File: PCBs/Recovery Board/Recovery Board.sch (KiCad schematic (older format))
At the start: 23 parts, among them J1 Conn_01x02, J2 Conn_01x02, J3 Conn_01x02, J4 Conn_01x02, J5 Conn_01x02, J6 Conn_01x02, U1 R-78E3.3-0.5, X1 XBee-S2C

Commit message: swapped all mounting holes with plated ones, fixed disconnected components on recovery, added the 4 decoupling caps to recovery, fixed silk screen on pads in instr, fixed traces connecting through pads on recovery and instr, moved q1 on instr, brought trace in near u2 on instr, switched u2 & u3 to hand solder on instr, fixed xbee screen on recovery, fixed connector labels on recovery, removed recovery dims past edge cuts, fixed pad mask clearance on recovery
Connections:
- net Stratologger_Switch+: now also J3.1 (Pin_1), S2.4 (DC_+); no longer J3.2 (Pin_2), S2.3 (DC_-)
- net Stratologger_Switch-: now also J3.2 (Pin_2), S2.3 (DC_-); no longer J3.1 (Pin_1), S2.4 (DC_+)
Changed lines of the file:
@@
 LIBS:fgpmmopa6h
 LIBS:sot-223
+LIBS:Placeholders
 LIBS:Recovery Board Parts
 LIBS:ap2204k-5
 LIBS:Recovery Board-cache
 LIBS:instrumentation_board_parts
+LIBS:instrumentation_board-cache
 EELAYER 25 0
 EELAYER END
@@
 	1    0    0    -1
 $EndComp
+Text GLabel 7550 1300 2    60   Input Italic 0
+Stratologger_Switch-
 Text GLabel 7550 900  2    60   Input Italic 0
-Stratologger_Switch-
-Text GLabel 7550 1300 2    60   Input Italic 0
 Stratologger_Switch+
 Text GLabel 2600 3300 2    60   Input ~ 0
@@
 Text GLabel 2600 2700 2    60   Input Italic 0
 Intrument_Arduino_Power
+Text GLabel 2600 2000 2    60   Input Italic 0
+Stratologger_Switch+
 Text GLabel 2600 2100 2    60   Input Italic 0
-Stratologger_Switch+
-Text GLabel 2600 2000 2    60   Input Italic 0
 Stratologger_Switch-
 $Comp

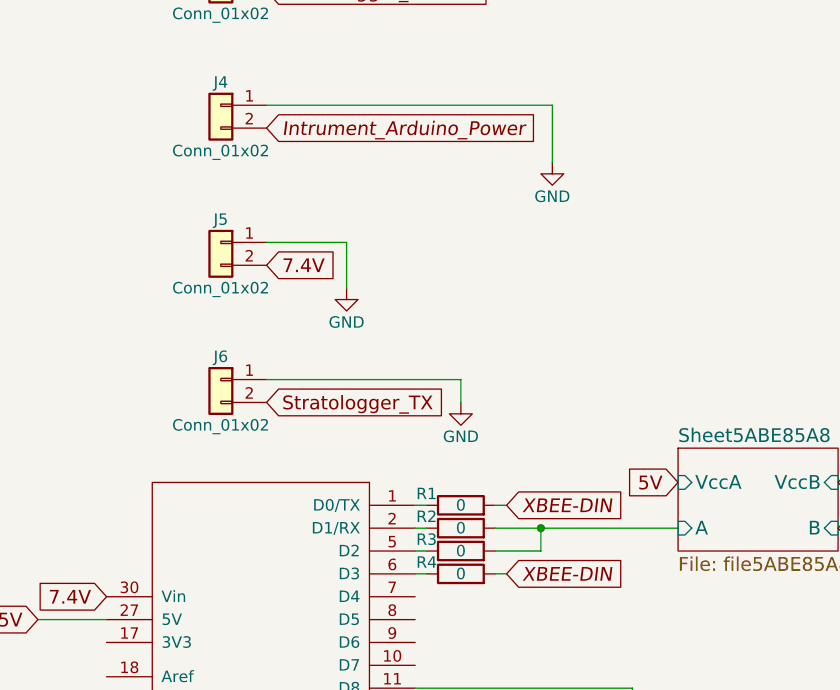
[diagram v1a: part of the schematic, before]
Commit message: Changed connectors for recovery board batteries
Added a second connector for the other battery
Moved connectors to top of board
Replaced footprint with JST-PH
Extended board width
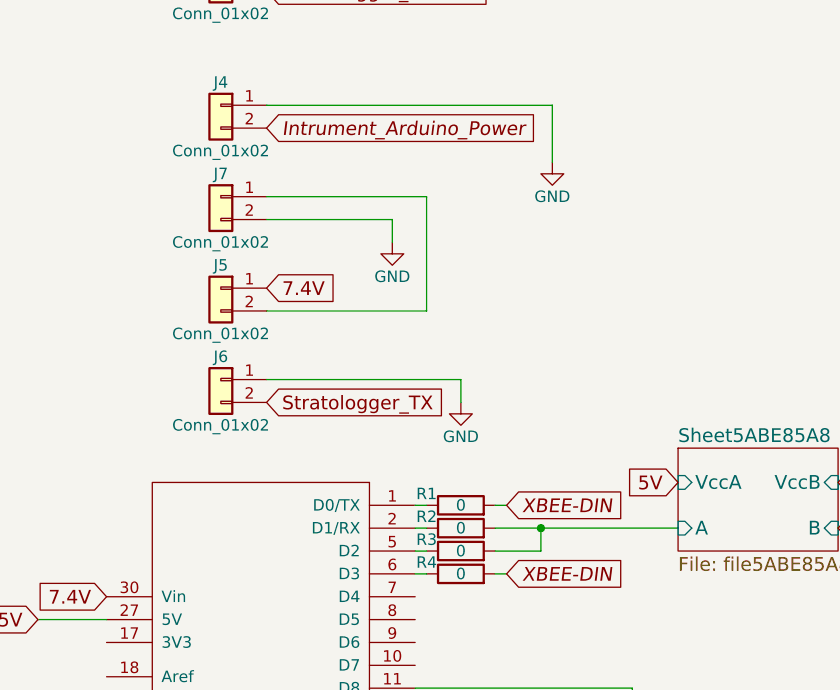
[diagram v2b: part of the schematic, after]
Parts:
- added J7: Conn_01x02, Connectors_JST:JST_PH_B2B-PH-K_02x2.00mm_Straight, symbol Conn_01x02
- J5: footprint Connectors_Molex:Molex_KK-6410-02_02x2.54mm_Straight -> Connectors_JST:JST_PH_B2B-PH-K_02x2.00mm_Straight
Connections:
- net 7.4V: now also J5.1 (Pin_1); no longer J5.2 (Pin_2)
- net GND: now also J7.2 (Pin_2); no longer J5.1 (Pin_1)
- new net: J5.2 (Pin_2), J7.1 (Pin_1)
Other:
- moved on the sheet: J5
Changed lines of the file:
@@
 Text GLabel 7550 900  2    60   Input Italic 0
 Stratologger_Switch+
-Text GLabel 2600 3300 2    60   Input ~ 0
+Text GLabel 2600 3400 2    60   Input ~ 0
 7.4V
 Text GLabel 7450 2000 2    60   Input ~ 0
@@
 L Conn_01x02 J5
 U 1 1 5A9A1806
-P 2400 3200
-F 0 "J5" H 2400 3300 50  0000 C CNN
-F 1 "Conn_01x02" H 2400 3000 50  0000 C CNN
-F 2 "Connectors_Molex:Molex_KK-6410-02_02x2.54mm_Straight" H 2400 3200 50  0001 C CNN
-F 3 "" H 2400 3200 50  0001 C CNN
-	1    2400 3200
+P 2400 3400
+F 0 "J5" H 2400 3500 50  0000 C CNN
+F 1 "Conn_01x02" H 2400 3200 50  0000 C CNN
+F 2 "Connectors_JST:JST_PH_B2B-PH-K_02x2.00mm_Straight" H 2400 3400 50  0001 C CNN
+F 3 "" H 2400 3400 50  0001 C CNN
+	1    2400 3400
 	-1   0    0    -1
 $EndComp
@@
 $EndComp
 $Comp
-L GND #PWR010
-U 1 1 5A9AE056
-P 2950 3400
-F 0 "#PWR010" H 2950 3150 50  0001 C CNN
-F 1 "GND" H 2950 3250 50  0000 C CNN
-F 2 "" H 2950 3400 50  0001 C CNN
-F 3 "" H 2950 3400 50  0001 C CNN
-	1    2950 3400
-	1    0    0    -1
-$EndComp
-$Comp
 L C C1
 U 1 1 5A9AEA7D
@@
 GoPro_Power
 $Comp
-L GND #PWR011
+L GND #PWR010
 U 1 1 5A9AF05A
 P 3850 2850
-F 0 "#PWR011" H 3850 2600 50  0001 C CNN
+F 0 "#PWR010" H 3850 2600 50  0001 C CNN
 F 1 "GND" H 3850 2700 50  0000 C CNN
 F 2 "" H 3850 2850 50  0001 C CNN
@@
 $EndComp
 $Comp
-L GND #PWR012
+L GND #PWR011
 U 1 1 5A9AF30B
 P 3350 1500
-F 0 "#PWR012" H 3350 1250 50  0001 C CNN
+F 0 "#PWR011" H 3350 1250 50  0001 C CNN
 F 1 "GND" H 3350 1350 50  0000 C CNN
 F 2 "" H 3350 1500 50  0001 C CNN
@@
 $EndComp
 $Comp
-L GND #PWR013
+L GND #PWR012
 U 1 1 5ABA400A
 P 8250 4650
-F 0 "#PWR013" H 8250 4400 50  0001 C CNN
+F 0 "#PWR012" H 8250 4400 50  0001 C CNN
 F 1 "GND" H 8250 4500 50  0000 C CNN
 F 2 "" H 8250 4650 50  0001 C CNN
@@
 $EndComp
 $Comp
-L GND #PWR014
+L GND #PWR013
 U 1 1 5ABA4092
 P 8500 4650
-F 0 "#PWR014" H 8500 4400 50  0001 C CNN
+F 0 "#PWR013" H 8500 4400 50  0001 C CNN
 F 1 "GND" H 8500 4500 50  0000 C CNN
 F 2 "" H 8500 4650 50  0001 C CNN
@@
 $EndComp
 $Comp
-L GND #PWR015
+L GND #PWR014
 U 1 1 5ABE78A1
 P 3450 3900
-F 0 "#PWR015" H 3450 3650 50  0001 C CNN
+F 0 "#PWR014" H 3450 3650 50  0001 C CNN
 F 1 "GND" H 3450 3750 50  0000 C CNN
 F 2 "" H 3450 3900 50  0001 C CNN
@@
 	1700 6300 1900 6300
 Wire Wire Line
-	2600 3200 2950 3200
-Wire Wire Line
-	2950 3200 2950 3400
-Wire Wire Line
 	2600 1250 3350 1250
 Wire Wire Line
@@
 $EndComp
 Wire Wire Line
-	4400 4450 3600 4450
+	3600 4450 4400 4450
 Wire Wire Line
 	3600 4550 3800 4550
@@
 Wire Wire Line
 	1900 4850 1600 4850
+$Comp
+L Conn_01x02 J7
+U 1 1 5AC93CD7
+P 2400 3000
+F 0 "J7" H 2400 3100 50  0000 C CNN
+F 1 "Conn_01x02" H 2400 2800 50  0000 C CNN
+F 2 "Connectors_JST:JST_PH_B2B-PH-K_02x2.00mm_Straight" H 2400 3000 50  0001 C CNN
+F 3 "" H 2400 3000 50  0001 C CNN
+	1    2400 3000
+	-1   0    0    -1
+$EndComp
+$Comp
+L GND #PWR015
+U 1 1 5AC93DCC
+P 3150 3200
+F 0 "#PWR015" H 3150 2950 50  0001 C CNN
+F 1 "GND" H 3150 3050 50  0000 C CNN
+F 2 "" H 3150 3200 50  0001 C CNN
+F 3 "" H 3150 3200 50  0001 C CNN
+	1    3150 3200
+	1    0    0    -1
+$EndComp
+Wire Wire Line
+	2600 3100 3150 3100
+Wire Wire Line
+	3150 3100 3150 3200
+Wire Wire Line
+	2600 3500 3300 3500
+Wire Wire Line
+	3300 3500 3300 3000
+Wire Wire Line
+	3300 3000 2600 3000
 $EndSCHEMATC

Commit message: Connector Changes
Flipped the transponder jst-ph connectors
Replaced the molex footprint on recovery with the correct one
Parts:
- J1, J2, J3, J4, J6: footprint Connectors_Molex:Molex_KK-6410-02_02x2.54mm_Straight -> molex:molex_kk_22-23-2021
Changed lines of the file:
@@
 F 0 "J4" H 2400 2700 50  0000 C CNN
 F 1 "Conn_01x02" H 2400 2400 50  0000 C CNN
-F 2 "Connectors_Molex:Molex_KK-6410-02_02x2.54mm_Straight" H 2400 2600 50  0001 C CNN
+F 2 "molex:molex_kk_22-23-2021" H 2400 2600 50  0001 C CNN
 F 3 "" H 2400 2600 50  0001 C CNN
 	1    2400 2600
@@
 F 0 "J3" H 2400 2100 50  0000 C CNN
 F 1 "Conn_01x02" H 2400 1800 50  0000 C CNN
-F 2 "Connectors_Molex:Molex_KK-6410-02_02x2.54mm_Straight" H 2400 2000 50  0001 C CNN
+F 2 "molex:molex_kk_22-23-2021" H 2400 2000 50  0001 C CNN
 F 3 "" H 2400 2000 50  0001 C CNN
 	1    2400 2000
@@
 F 0 "J2" H 2400 1350 50  0000 C CNN
 F 1 "Conn_01x02" H 2400 1050 50  0000 C CNN
-F 2 "Connectors_Molex:Molex_KK-6410-02_02x2.54mm_Straight" H 2400 1250 50  0001 C CNN
+F 2 "molex:molex_kk_22-23-2021" H 2400 1250 50  0001 C CNN
 F 3 "" H 2400 1250 50  0001 C CNN
 	1    2400 1250
@@
 F 0 "J1" H 2400 800 50  0000 C CNN
 F 1 "Conn_01x02" H 2400 500 50  0000 C CNN
-F 2 "Connectors_Molex:Molex_KK-6410-02_02x2.54mm_Straight" H 2400 700 50  0001 C CNN
+F 2 "molex:molex_kk_22-23-2021" H 2400 700 50  0001 C CNN
 F 3 "" H 2400 700 50  0001 C CNN
 	1    2400 700
@@
 F 0 "J6" H 2400 3900 50  0000 C CNN
 F 1 "Conn_01x02" H 2400 3600 50  0000 C CNN
-F 2 "Connectors_Molex:Molex_KK-6410-02_02x2.54mm_Straight" H 2400 3800 50  0001 C CNN
+F 2 "molex:molex_kk_22-23-2021" H 2400 3800 50  0001 C CNN
 F 3 "" H 2400 3800 50  0001 C CNN
 	1    2400 3800
